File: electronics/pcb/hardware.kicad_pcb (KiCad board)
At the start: 4 copper layers, 59 x 53 mm, 144 parts, among them J1 Micro_SD_Card_Det_Hirose_DM3AT, J2 USB_A, J3 USB_A, J5 Conn_02x10_Odd_Even, U1 AS4C512M16D3L-12BIN, U2 A33, U3 TPS62095RGTR, U4 TPS62095RGTR, U5 TPS62095RGTR, U6 TPS62095RGTR, U7 AP131-25, Y1 24Mhz, Y2 32.768khz

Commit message: Schematic review.
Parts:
- added C32: 100nF, Capacitor_SMD:C_0402_1005Metric, B.Cu at (135.1, 106.6)
- C2: moved to B.Cu
- moved C2 6.33 mm to (137.6, 98.6), turned to 270 degrees
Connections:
- net Net-(J2-Pad2) renamed /gpio/USB-DM0
- net Net-(J2-Pad3) renamed /gpio/USB-DP0
- net Net-(J3-Pad2) renamed /gpio/USB-DM1
- net Net-(J3-Pad3) renamed /gpio/USB-DP1
- U2 pad L4: /ram/!CAS -> /ram/!RAS
- U2 pad M3: /ram/!RAS -> /ram/!CAS
- U2 pad R1: /ram/!UDQS -> /ram/UDQS
- U2 pad T1: /ram/UDQS -> /ram/!UDQS
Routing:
- net /ram/!RAS: track 37.9 -> 41.1 mm
- net /ram/UDQS: track 14.7 -> 12.8 mm
- net /ram/!UDQS: track 14.6 -> 13.4 mm
- net +1V35: track 69.5 -> 68.9 mm, vias 26 -> 25
- net GND: vias 55 -> 56

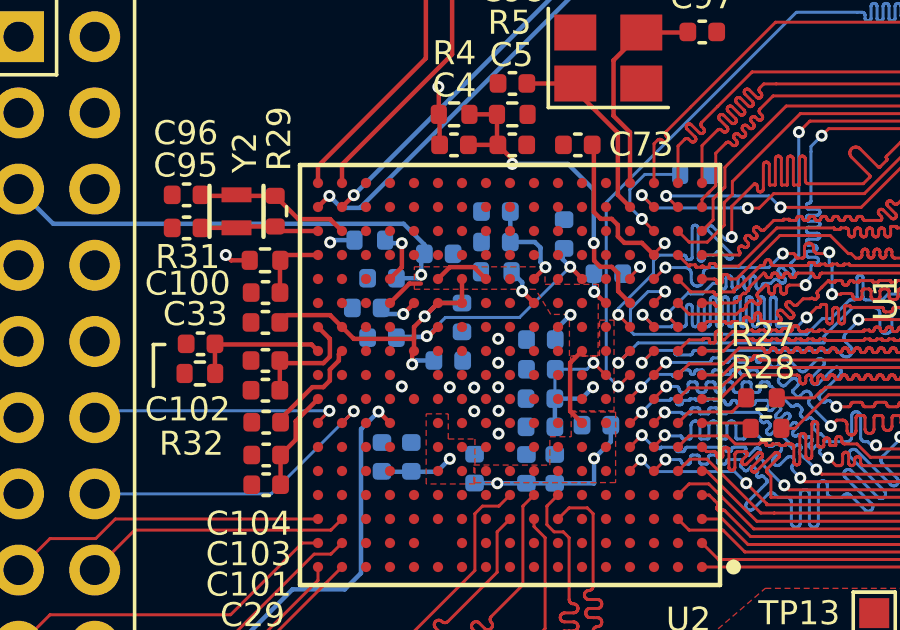
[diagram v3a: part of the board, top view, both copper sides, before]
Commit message: Reworked 3.3V
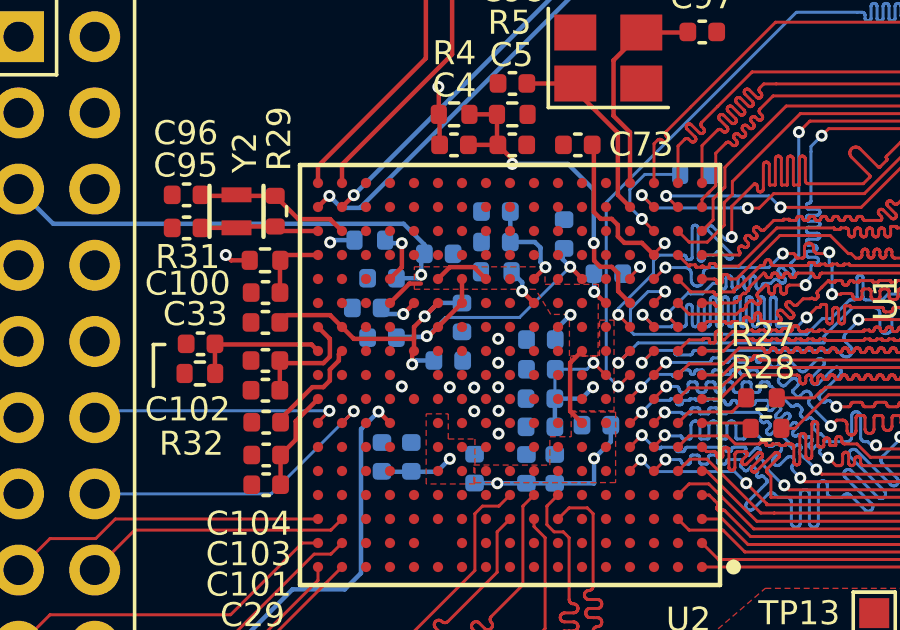
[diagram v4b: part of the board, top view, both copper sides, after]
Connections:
- U2 pad M11: +3V0 -> +3V3
- U2 pad N11: +3V0 -> +3V3
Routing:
- net +3V3: track 51.8 -> 53.8 mm
- net +3V0: track 24.8 -> 23.2 mm
